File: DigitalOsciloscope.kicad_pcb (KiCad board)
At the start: 4 copper layers, 150 x 150 mm, 413 parts, among them J1 Conn_Coaxial, J10 Conn_01x02_Pin, J11 Conn_01x02_Pin, J12 Conn_01x02_Pin, J14 Conn_01x02_Pin, J2 Conn_Coaxial, J3 Conn_Coaxial, J4 Conn_01x03_Pin, J5 Conn_01x03_Pin, J6 Screw_Terminal_01x02, J7 Screw_Terminal_01x03, J8 Conn_01x03_Pin, J9 Conn_01x03_Pin, K1 TQ2-5V, K2 TQ2-5V, K3 TQ2-5V, K4 TQ2-5V, K5 TQ2-5V, K6 TQ2-5V, K7 TQ2-5V, Q1 2N7002, Q2 2N7002, Q3 2N7002, Q4 2N7002, Q6 2N7002, Q8 2N7002, Q9 2N7002, U1 TL072, U10 P0082_BOTTOMMOUNT, U11 NUCLEOH723ZG, U12 ADP7182AUJZ, U13 ADP7182AUJZ, U14 AZ1117-ADJ, U15 AZ1117-ADJ, U16 AZ1117-ADJ, U17 DAC61408RHAR, U18 AZ1117-ADJ, U19 AZ1117-ADJ, U2 OPA656U, U3 OPA656U, U4 AD8611ARZ, U5 AD8337BCPZ-REEL-ND, U6 AD8337BCPZ-REEL-ND, U7 AD8138ARZ, U8 AD8138ARZ, U9 LTC2299xUP, Y1 XLL735080.000000I

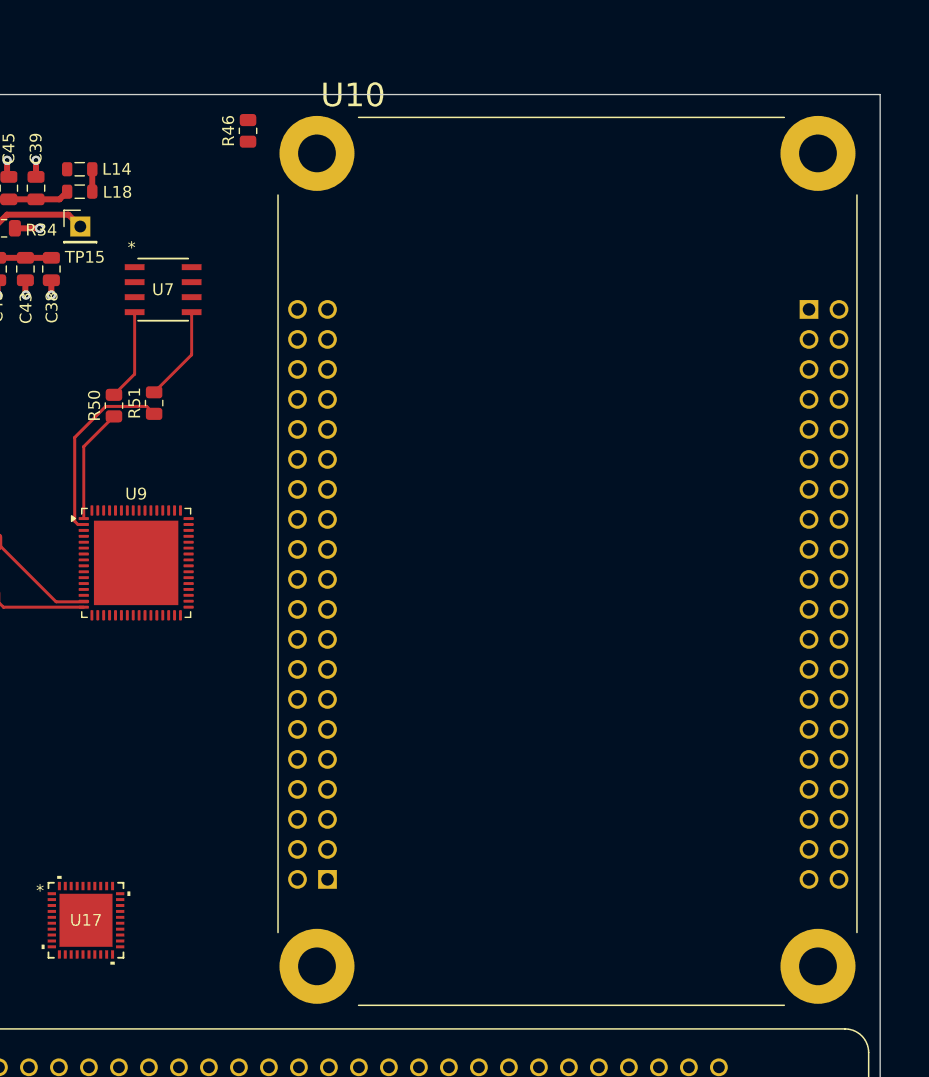
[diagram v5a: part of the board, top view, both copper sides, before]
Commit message: Save work before changing the pin header of FPGA connected to LTC2299
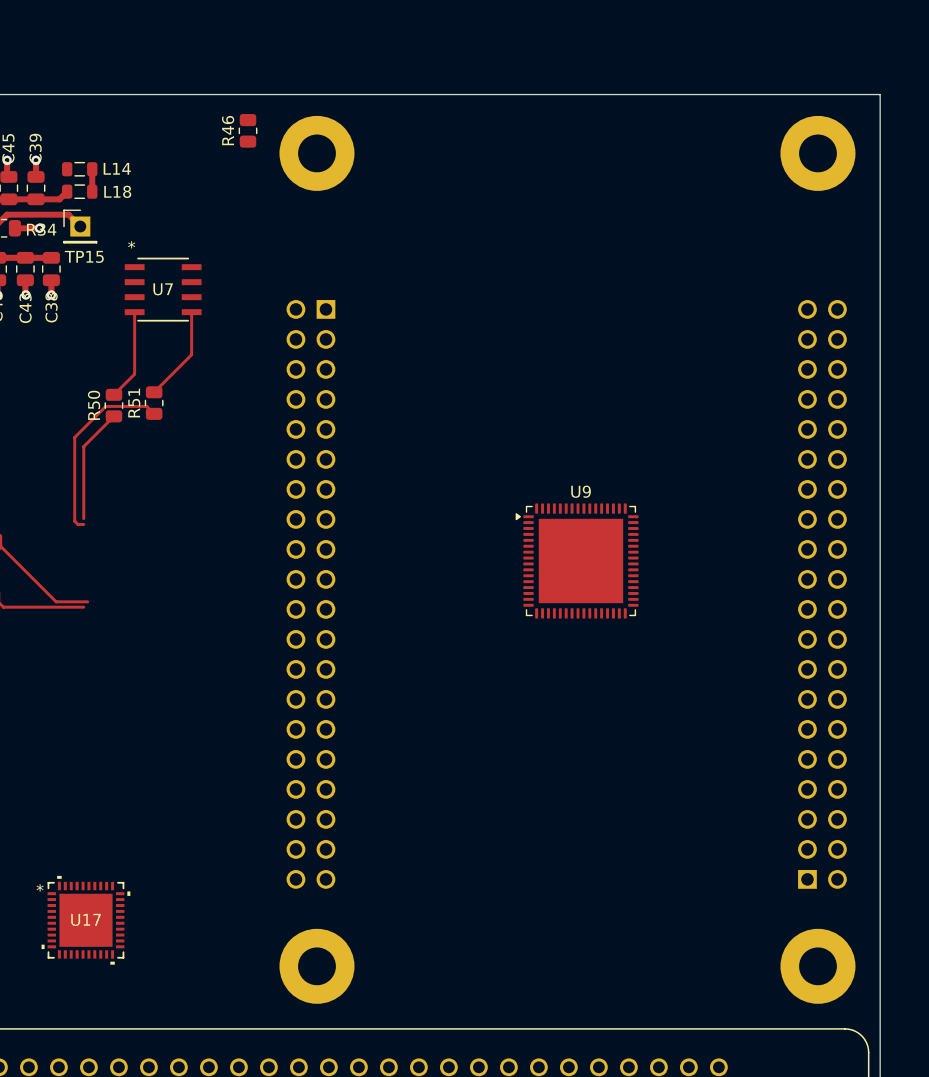
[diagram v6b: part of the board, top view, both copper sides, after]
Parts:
- U10: moved to B.Cu
- moved U9 37.7 mm to (247.1, 92.0)
- turned U10 to 180 degrees
